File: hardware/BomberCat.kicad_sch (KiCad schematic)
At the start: 87 parts, among them J1 Battery, J2 SWD, J3 MAGSPOOF, P1 USB_C_Plug_USB2.0, Q1 DMG3415U-7, SW1 RESET, SW2 GPIO, SW3 ON, U1 PN7150B0HN_C11002E-PN7150B0HN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, U2 RP2040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

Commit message: update component groups
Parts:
- C11, C22, C23, C24, C25, C26, C27, C28, C29, C3, C30, C31, C32, C4, C5, C6, C7, C8, C9: footprint Capacitor_SMD:C_0603_1608Metric_Pad1.08x0.95mm_HandSolder -> Capacitor_SMD:C_0603_1608Metric
- C34: footprint Capacitor_SMD:C_0805_2012Metric_Pad1.15x1.40mm_HandSolder -> Capacitor_SMD:C_0603_1608Metric
- L3: footprint BomberCat:RP2040-QFN-56 -> (none)
- R1, R11, R12, R13, R14, R15, R16, R18, R19, R2, R21, R22, R4, R5, R6, R7, R8: footprint Resistor_SMD:R_0603_1608Metric_Pad1.05x0.95mm_HandSolder -> Resistor_SMD:R_0603_1608Metric
- U2: footprint RP2040:RP2040-QFN-56 -> BomberCat:RP2040-QFN-56
- gave numbers to parts that had none: 1
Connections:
- net +BATT: no longer C34.1
- net at SW4.2 (B), U7.6 (VDD): now also C34.1
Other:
- moved on the sheet: C34

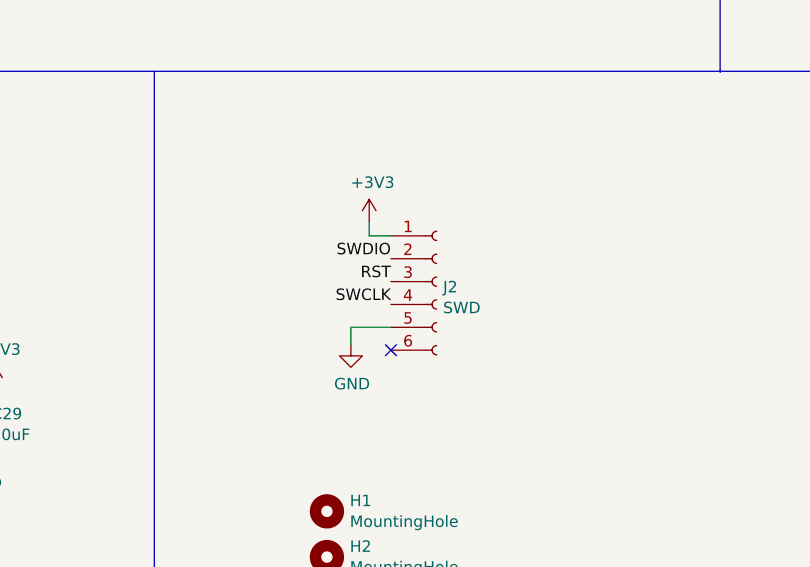
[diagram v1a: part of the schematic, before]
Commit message: Add grouped blocks for floorplan
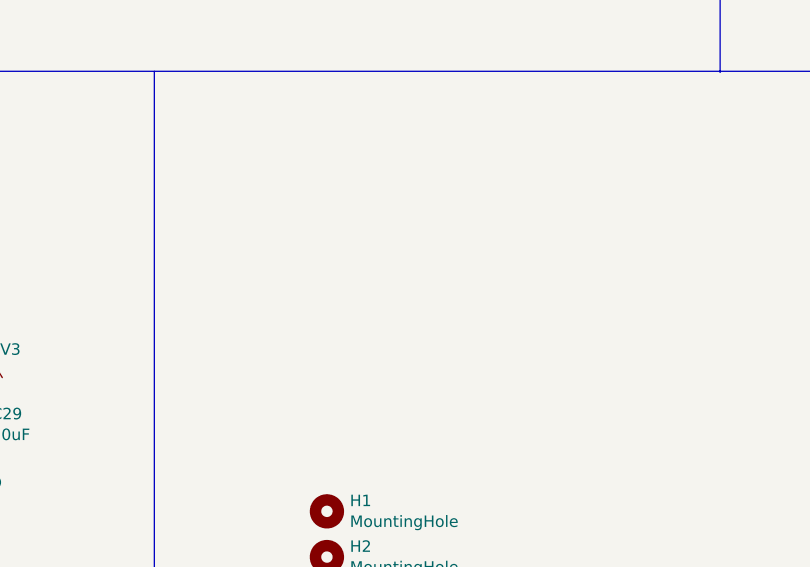
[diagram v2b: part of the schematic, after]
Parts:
- removed J2: SWD, Connector:Tag-Connect_TC2030-IDC-NL_2x03_P1.27mm_Vertical, symbol Connector:Conn_01x06_Female
- U6: manf# W25Q16JVUXIQ -> W25Q16JVUUIQ
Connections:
- no-connect marks 42 -> 41
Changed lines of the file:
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@@
   (no_connect (at 22.606 271.526))
   (no_connect (at 358.14 59.69))
-  (no_connect (at 277.368 245.745))
   (no_connect (at 111.76 195.58))
   (no_connect (at 111.76 193.04))
@@
     (stroke (width 0) (type default) (color 0 0 0 0))
   )
-  (wire (pts (xy 277.368 243.205) (xy 272.923 243.205))
-    (stroke (width 0) (type default) (color 0 0 0 0))
-  )
   (wire (pts (xy 88.9 76.2) (xy 89.916 76.2))
     (stroke (width 0) (type default) (color 0 0 0 0))
@@
     (stroke (width 0) (type default) (color 0 0 0 0))
   )
-  (wire (pts (xy 274.955 233.045) (xy 277.368 233.045))
-    (stroke (width 0) (type default) (color 0 0 0 0))
-  )
   (polyline (pts (xy 67.056 215.011) (xy 67.056 284.734))
     (stroke (width 0) (type default) (color 0 0 0 0))
@@
     (stroke (width 0) (type default) (color 0 0 0 0))
   )
-  (wire (pts (xy 274.955 231.521) (xy 274.955 233.045))
-    (stroke (width 0) (type default) (color 0 0 0 0))
-  )
   (wire (pts (xy 135.89 149.352) (xy 135.89 148.336))
     (stroke (width 0) (type default) (color 0 0 0 0))
@@
     (stroke (width 0) (type default) (color 0 0 0 0))
   )
-  (wire (pts (xy 272.923 243.205) (xy 272.923 245.11))
-    (stroke (width 0) (type default) (color 0 0 0 0))
-  )
   (wire (pts (xy 238.506 114.3) (xy 238.506 117.856))
     (stroke (width 0) (type default) (color 0 0 0 0))
@@
     (effects (font (size 2.2606 2.2606)) (justify left bottom))
   )
-  (label "RST" (at 277.368 238.125 180)
-    (effects (font (size 1.27 1.27)) (justify right bottom))
-  )
   (label "B_ADC" (at 114.3 187.96 0)
     (effects (font (size 1.27 1.27)) (justify left bottom))
@@
     (effects (font (size 1.27 1.27)) (justify left bottom))
   )
-  (label "SWCLK" (at 277.368 240.665 180)
-    (effects (font (size 1.27 1.27)) (justify right bottom))
-  )
   (label "QSPI_CS" (at 339.344 46.99 180)
     (effects (font (size 1.27 1.27)) (justify right bottom))
@@
     (effects (font (size 1.27 1.27)) (justify right bottom))
   )
-  (label "SWDIO" (at 277.368 235.585 180)
-    (effects (font (size 1.27 1.27)) (justify right bottom))
-  )
   (label "SCK" (at 114.554 154.94 0)
     (effects (font (size 1.27 1.27)) (justify left bottom))
@@
     (pin "2")
   )
-  (symbol (lib_id "power:+3V3") (at 274.955 231.521 0) (unit 1)
-    (in_bom yes) (on_board yes)
-    (property "Reference" "#PWR067" (id 0) (at 274.955 235.331 0)
-      (effects (font (size 1.27 1.27)) hide)
-    )
-    (property "Value" "+3V3" (id 1) (at 275.336 227.1268 0))
-    (property "Footprint" "" (id 2) (at 274.955 231.521 0)
-      (effects (font (size 1.27 1.27)) hide)
-    )
-    (property "Datasheet" "" (id 3) (at 274.955 231.521 0)
-      (effects (font (size 1.27 1.27)) hide)
-    )
-    (pin "1")
-  )
   (symbol (lib_id "power:GND") (at 88.138 254.508 0) (unit 1)
     (in_bom yes) (on_board yes)
@@
     (pin "2")
   )
-  (symbol (lib_id "power:GND") (at 272.923 245.11 0) (unit 1)
-    (in_bom yes) (on_board yes)
-    (property "Reference" "#PWR066" (id 0) (at 272.923 251.46 0)
-      (effects (font (size 1.27 1.27)) hide)
-    )
-    (property "Value" "GND" (id 1) (at 273.05 249.5042 0))
-    (property "Footprint" "" (id 2) (at 272.923 245.11 0)
-      (effects (font (size 1.27 1.27)) hide)
-    )
-    (property "Datasheet" "" (id 3) (at 272.923 245.11 0)
-      (effects (font (size 1.27 1.27)) hide)
-    )
-    (pin "1")
-  )
   (symbol (lib_id "power:GND") (at 158.623 78.867 0) (unit 1)
     (in_bom yes) (on_board yes)
@@
     (pin "2")
   )
-  (symbol (lib_id "Connector:Conn_01x06_Female") (at 282.448 238.125 0) (unit 1)
-    (in_bom yes) (on_board yes)
-    (property "Reference" "J2" (id 0) (at 283.1592 238.7346 0)
-      (effects (font (size 1.27 1.27)) (justify left))
-    )
-    (property "Value" "SWD" (id 1) (at 283.1592 241.046 0)
-      (effects (font (size 1.27 1.27)) (justify left))
-    )
-    (property "Footprint" "Connector:Tag-Connect_TC2030-IDC-NL_2x03_P1.27mm_Vertical" (id 2) (at 282.448 238.125 0)
-      (effects (font (size 1.27 1.27)) hide)
-    )
-    (property "Datasheet" "~" (id 3) (at 282.448 238.125 0)
-      (effects (font (size 1.27 1.27)) hide)
-    )
-    (property "LCSC#" "-" (id 4) (at 282.448 238.125 0)
-      (effects (font (size 1.27 1.27)) hide)
-    )
-    (property "manf#" "-" (id 5) (at 282.448 238.125 0)
-      (effects (font (size 1.27 1.27)) hide)
-    )
-    (property "provedor" "-" (id 6) (at 282.448 238.125 0)
-      (effects (font (size 1.27 1.27)) hide)
-    )
-    (pin "1")
-    (pin "2")
-    (pin "3")
-    (pin "4")
-    (pin "5")
-    (pin "6")
-  )
   (symbol (lib_id "Device:R_Small") (at 340.614 41.656 0) (unit 1)
     (in_bom yes) (on_board yes)
@@
       (effects (font (size 1.27 1.27)) hide)
     )
-    (property "manf#" "W25Q16JVUXIQ" (id 4) (at 355.6 49.53 0)
+    (property "manf#" "W25Q16JVUUIQ" (id 4) (at 355.6 49.53 0)
       (effects (font (size 1.27 1.27)) hide)
     )
@@
       (reference "#PWR065") (unit 1) (value "GND") (footprint "")
     )
-    (path "/41589aa4-8207-48cd-9604-d470a79f1b09"
-      (reference "#PWR066") (unit 1) (value "GND") (footprint "")
-    )
-    (path "/161f4512-e880-4e19-93e2-a71f03b372cc"
-      (reference "#PWR067") (unit 1) (value "+3V3") (footprint "")
-    )
     (path "/b912cb03-6506-4ea0-b59e-bd5dc701fd6d"
       (reference "#PWR068") (unit 1) (value "+3V3") (footprint "")
@@
       (reference "J1") (unit 1) (value "Battery") (footprint "Connector_PinSocket_2.54mm:PinSocket_2x01_P2.54mm_Vertical_SMD")
     )
-    (path "/52ce673b-f69b-463d-a086-3ed9f9e00269"
-      (reference "J2") (unit 1) (value "SWD") (footprint "Connector:Tag-Connect_TC2030-IDC-NL_2x03_P1.27mm_Vertical")
-    )
     (path "/c0799fc0-14a9-4c3d-af23-f92bbaae8e80"

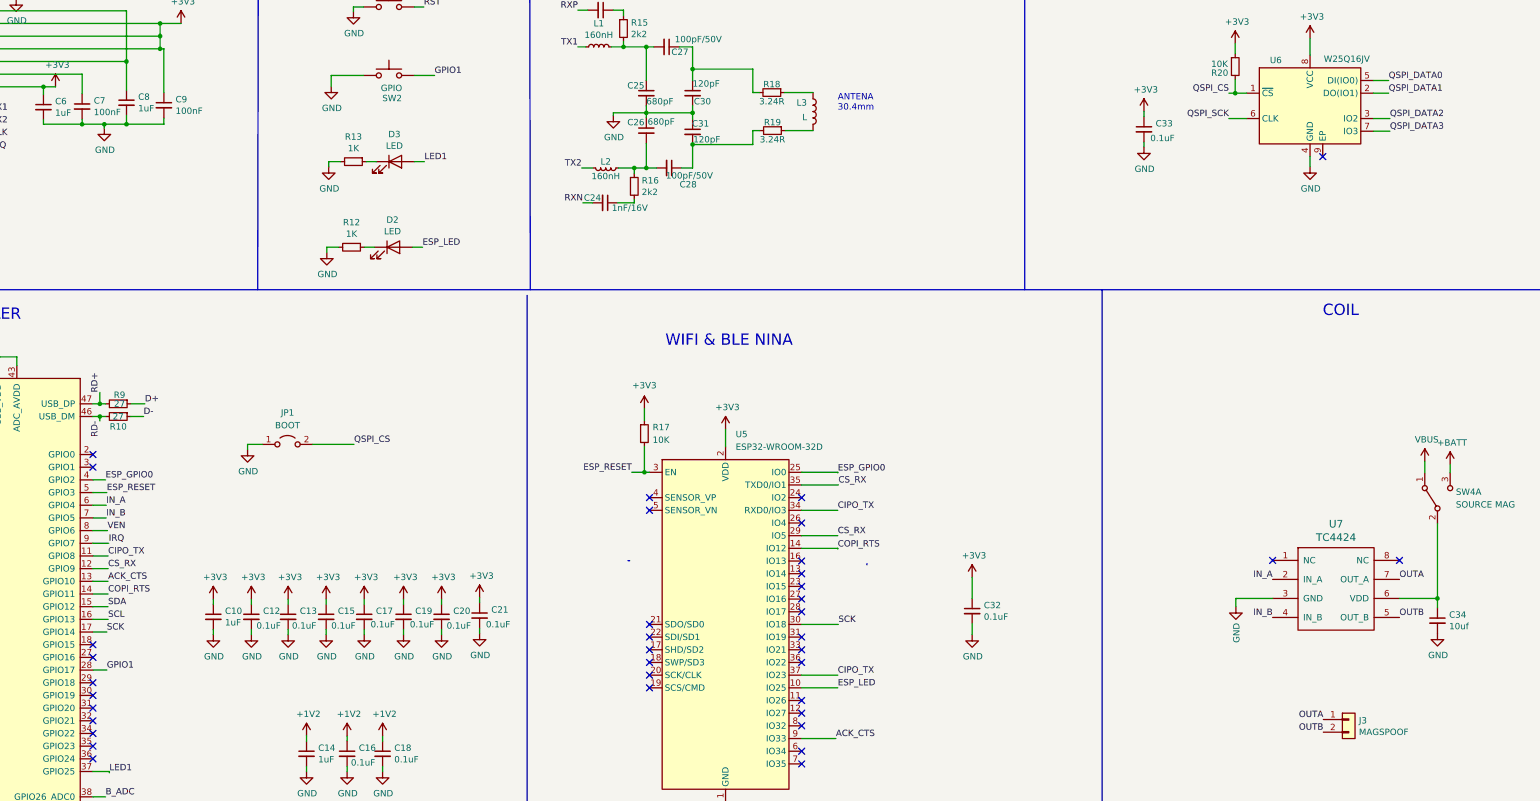
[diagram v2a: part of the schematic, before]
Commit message: add layout waiting for switch's
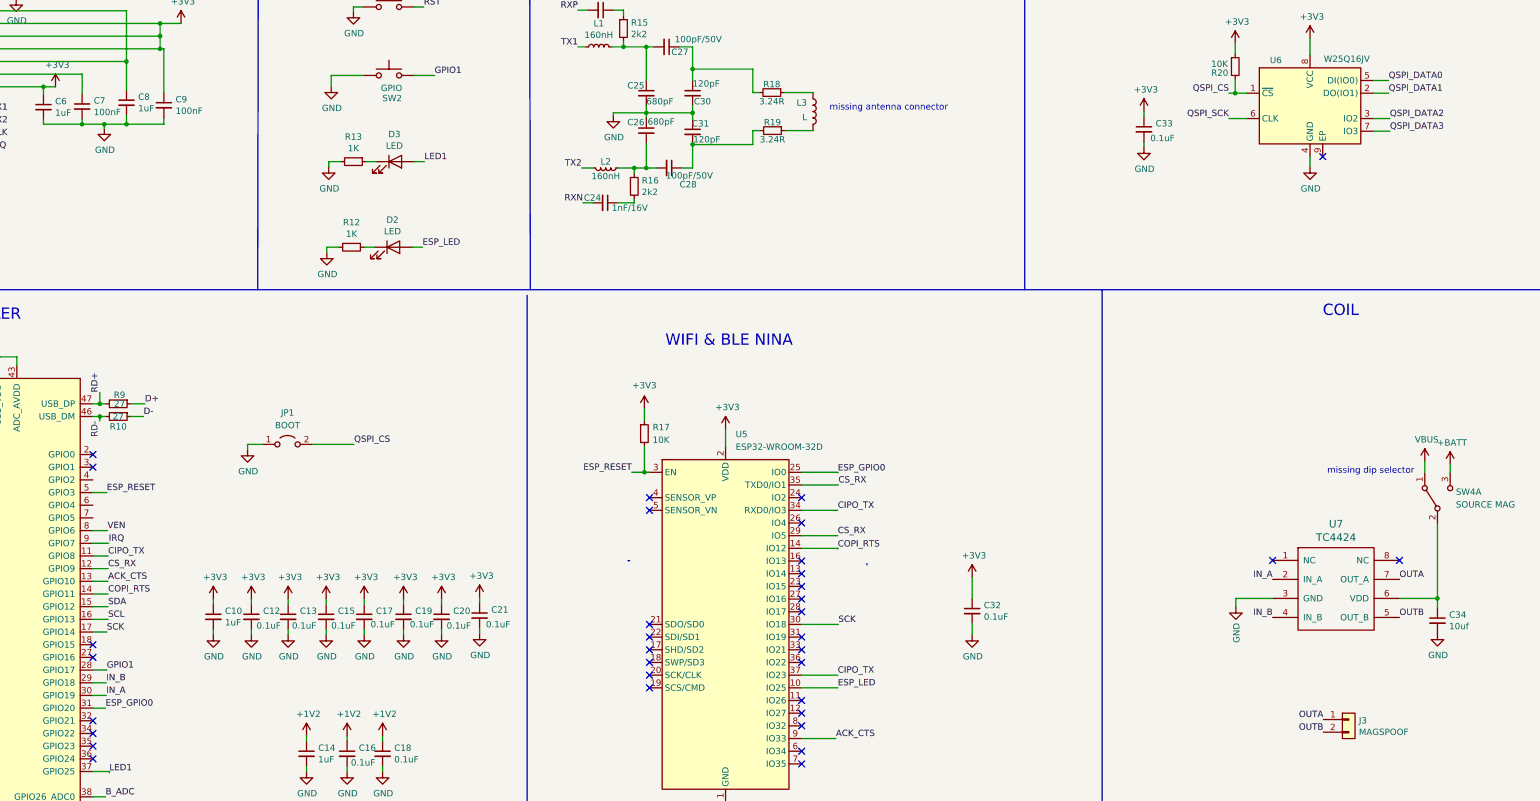
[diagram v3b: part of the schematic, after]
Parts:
- J1: footprint Connector_PinSocket_2.54mm:PinSocket_2x01_P2.54mm_Vertical_SMD -> Connector_PinHeader_2.54mm:PinHeader_1x02_P2.54mm_Vertical
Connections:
- net ESP_GPIO0: now also U2.31 (GPIO20); no longer U2.4 (GPIO2)
- net IN_A: now also U2.30 (GPIO19); no longer U2.6 (GPIO4)
- net IN_B: now also U2.29 (GPIO18); no longer U2.7 (GPIO5)
- no-connect marks 41 -> 38
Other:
- note added: "missing antenna connector"
- note added: "missing dip selector"
- note removed: "ANTENA 30.4mm"
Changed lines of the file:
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@@
   (no_connect (at 111.76 157.48))
   (no_connect (at 111.76 172.72))
-  (no_connect (at 111.76 170.18))
-  (no_connect (at 111.76 167.64))
-  (no_connect (at 111.76 165.1))
   (no_connect (at 111.76 160.02))
   (no_connect (at 253.746 161.036))
@@
     (stroke (width 0) (type default) (color 0 0 0 0))
   )
-  (wire (pts (xy 111.76 129.54) (xy 114.427 129.54))
+  (wire (pts (xy 111.76 167.64) (xy 114.427 167.64))
     (stroke (width 0) (type default) (color 0 0 0 0))
   )
@@
     (stroke (width 0) (type default) (color 0 0 0 0))
   )
-  (wire (pts (xy 111.76 124.46) (xy 114.3 124.46))
+  (wire (pts (xy 111.76 170.18) (xy 114.3 170.18))
     (stroke (width 0) (type default) (color 0 0 0 0))
   )
@@
     (stroke (width 0) (type default) (color 0 0 0 0))
   )
-  (wire (pts (xy 111.76 132.08) (xy 114.427 132.08))
+  (wire (pts (xy 111.76 165.1) (xy 114.427 165.1))
     (stroke (width 0) (type default) (color 0 0 0 0))
   )
@@
     (stroke (width 0) (type default) (color 0 0 0 0))
   )
+  (text "missing dip selector" (at 359.029 123.444 0)
+    (effects (font (size 1.27 1.27)) (justify left bottom))
+  )
+  (text "missing antenna connector\n" (at 259.334 50.673 0)
+    (effects (font (size 1.27 1.27)) (justify left bottom))
+  )
   (text "COIL" (at 358.14 91.948 0)
     (effects (font (size 2.2606 2.2606)) (justify left bottom))
@@
     (effects (font (size 2.2606 2.2606)) (justify left bottom))
   )
-  (text "ANTENA\n30.4mm\n" (at 260.985 50.673 0)
-    (effects (font (size 1.27 1.27)) (justify left bottom))
-  )
   (text "LEDS & BUTTONS" (at 157.099 16.891 0)
     (effects (font (size 2.2606 2.2606)) (justify left bottom))
@@
     (effects (font (size 1.27 1.27)) (justify left bottom))
   )
-  (label "ESP_GPIO0" (at 114.3 124.46 0)
+  (label "ESP_GPIO0" (at 114.3 170.18 0)
     (effects (font (size 1.27 1.27)) (justify left bottom))
   )
@@
     (effects (font (size 1.27 1.27)) (justify left bottom))
   )
-  (label "IN_B" (at 114.427 132.08 0)
+  (label "IN_B" (at 114.427 165.1 0)
     (effects (font (size 1.27 1.27)) (justify left bottom))
   )
@@
     (effects (font (size 1.27 1.27)) (justify left bottom))
   )
-  (label "IN_A" (at 114.427 129.54 0)
+  (label "IN_A" (at 114.427 167.64 0)
     (effects (font (size 1.27 1.27)) (justify left bottom))
   )
@@
       (effects (font (size 1.27 1.27)) (justify left))
     )
-    (property "Footprint" "Connector_PinSocket_2.54mm:PinSocket_2x01_P2.54mm_Vertical_SMD" (id 2) (at 162.052 250.19 0)
+    (property "Footprint" "Connector_PinHeader_2.54mm:PinHeader_1x02_P2.54mm_Vertical" (id 2) (at 162.052 250.19 0)
       (effects (font (size 1.27 1.27)) hide)
     )
@@
     )
     (path "/1e4bd640-5ebe-4c8a-92f8-b0ee934b378b"
-      (reference "J1") (unit 1) (value "Battery") (footprint "Connector_PinSocket_2.54mm:PinSocket_2x01_P2.54mm_Vertical_SMD")
+      (reference "J1") (unit 1) (value "Battery") (footprint "Connector_PinHeader_2.54mm:PinHeader_1x02_P2.54mm_Vertical")
     )
     (path "/c0799fc0-14a9-4c3d-af23-f92bbaae8e80"
